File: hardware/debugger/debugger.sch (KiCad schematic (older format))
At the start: 23 parts, among them J1 DB37_Male, J2 DB37_Male, U1 Teensy3.6, U10 PI6C49CB04AQ, U11 PI6C49CB04AQ, U2 SN74CBTLV3257PWR, U3 SN74CBTLV3257PWR, U4 SN74CBTLV3257PWR, U5 SN74CBTLV3257PWR, U6 SN74CBTLV3257PWR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

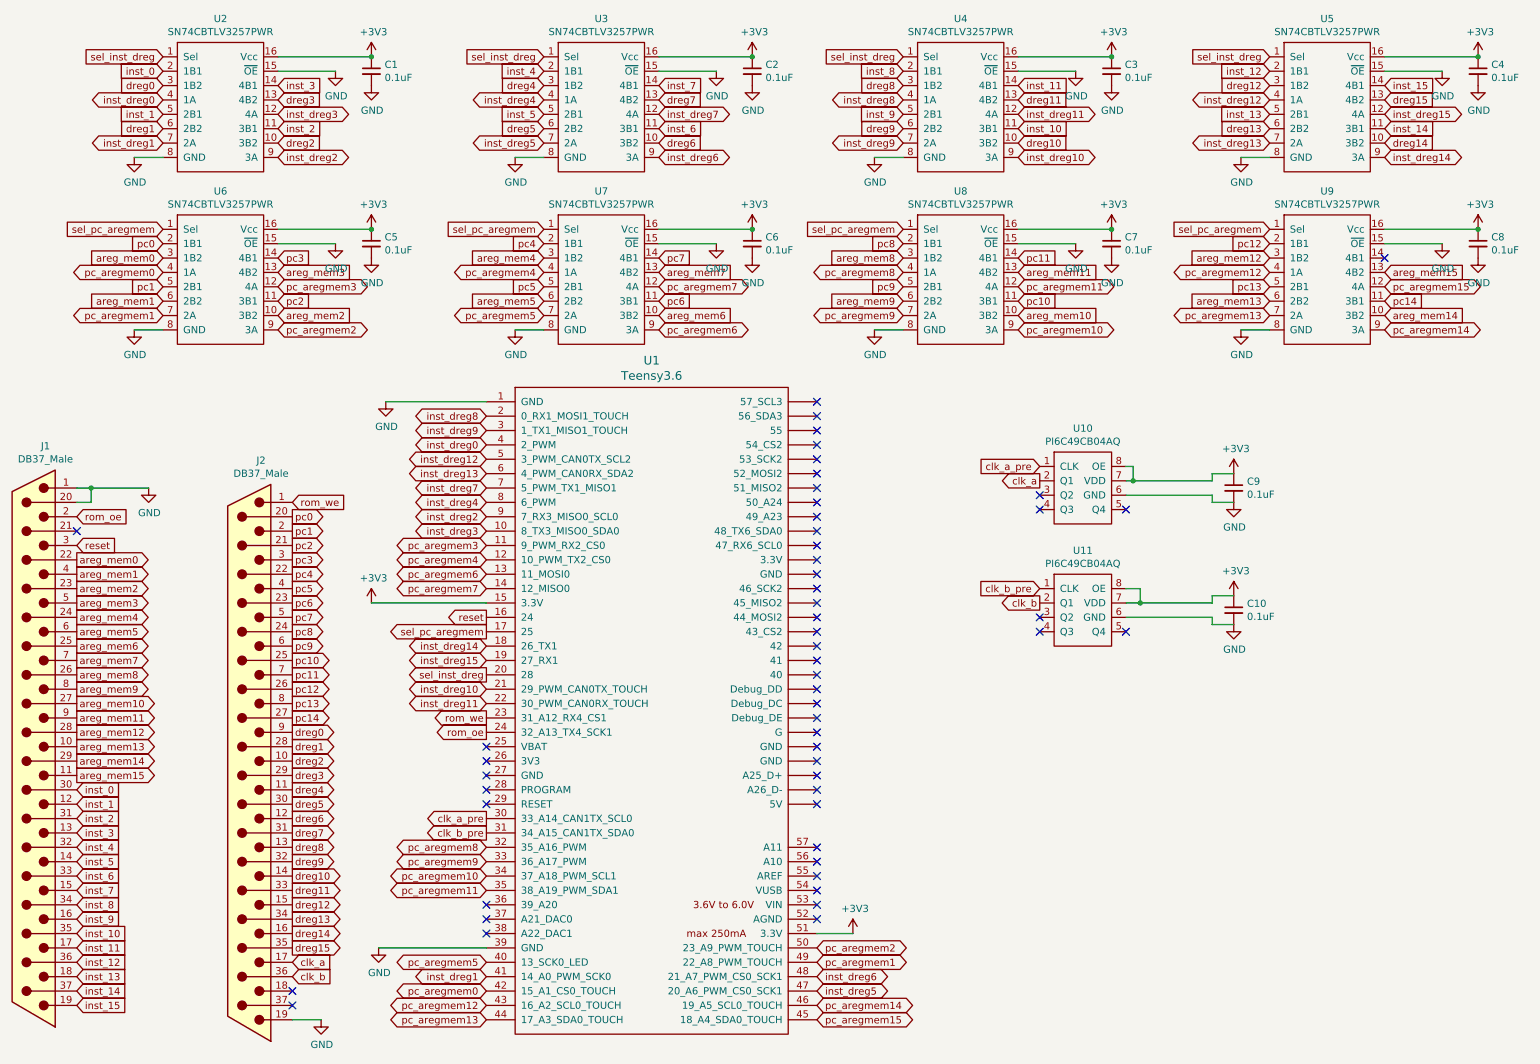
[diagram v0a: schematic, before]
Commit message: Debugger updated to Teensy 4.1 with magjack for ethernet. Updated motherboard<>debugger pinout to include 3.3v source
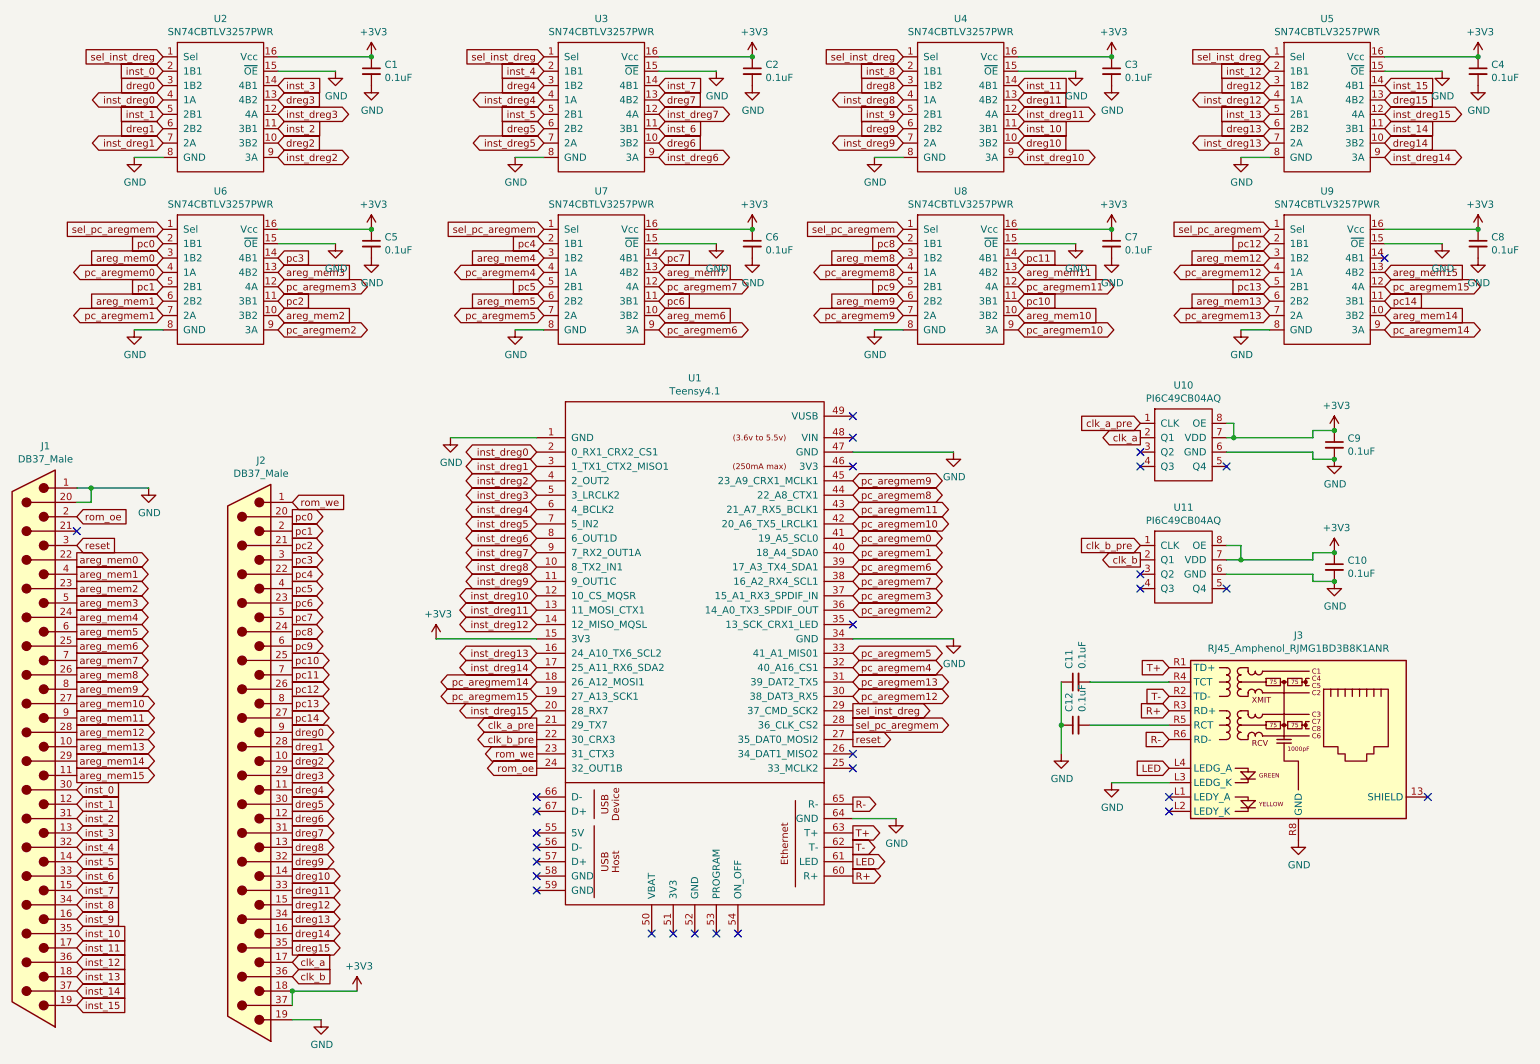
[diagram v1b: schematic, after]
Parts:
- removed U1: Teensy3.6, nandirl logo:Teensy35_36, symbol teensy:Teensy3.6
- added C11, C12: 0.1uF, Capacitor_SMD:C_1206_3216Metric, symbol Device:C_Small
- added J3: RJ45_Amphenol_RJMG1BD3B8K1ANR, Connector_RJ:RJ45_Amphenol_RJMG1BD3B8K1ANR, symbol Connector:RJ45_Amphenol_RJMG1BD3B8K1ANR
- added U1: Teensy4.1, nandirl logo:Teensy41, symbol teensy:Teensy4.1
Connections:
- net +3V3: now also J2.18, J2.37, U1.15 (3V3)
- net GND: now also C11.1, C12.1, J3.L3 (LEDG_K), J3.R8 (GND), U1.1 (GND), U1.34 (GND), U1.47 (GND), U1.64 (GND)
- net clk_a_pre: now also U1.21 (29_TX7)
- net clk_b_pre: now also U1.22 (30_CRX3)
- net inst_dreg0: now also U1.2 (0_RX1_CRX2_CS1)
- net inst_dreg1: now also U1.3 (1_TX1_CTX2_MISO1)
- net inst_dreg10: now also U1.12 (10_CS_MQSR)
- net inst_dreg11: now also U1.13 (11_MOSI_CTX1)
- net inst_dreg12: now also U1.14 (12_MISO_MQSL)
- net inst_dreg13: now also U1.16 (24_A10_TX6_SCL2)
- net inst_dreg14: now also U1.17 (25_A11_RX6_SDA2)
- net inst_dreg15: now also U1.20 (28_RX7)
- net inst_dreg2: now also U1.4 (2_OUT2)
- net inst_dreg3: now also U1.5 (3_LRCLK2)
- net inst_dreg4: now also U1.6 (4_BCLK2)
- net inst_dreg5: now also U1.7 (5_IN2)
- net inst_dreg6: now also U1.8 (6_OUT1D)
- net inst_dreg7: now also U1.9 (7_RX2_OUT1A)
- net inst_dreg8: now also U1.10 (8_TX2_IN1)
- net inst_dreg9: now also U1.11 (9_OUT1C)
- net pc_aregmem0: now also U1.41 (19_A5_SCL0)
- net pc_aregmem1: now also U1.40 (18_A4_SDA0)
- net pc_aregmem10: now also U1.42 (20_A6_TX5_LRCLK1)
- net pc_aregmem11: now also U1.43 (21_A7_RX5_BCLK1)
- net pc_aregmem12: now also U1.30 (38_DAT3_RX5)
- net pc_aregmem13: now also U1.31 (39_DAT2_TX5)
- net pc_aregmem14: now also U1.18 (26_A12_MOSI1)
- net pc_aregmem15: now also U1.19 (27_A13_SCK1)
- net pc_aregmem2: now also U1.36 (14_A0_TX3_SPDIF_OUT)
- net pc_aregmem3: now also U1.37 (15_A1_RX3_SPDIF_IN)
- net pc_aregmem4: now also U1.32 (40_A16_CS1)
- net pc_aregmem5: now also U1.33 (41_A1_MIS01)
- net pc_aregmem6: now also U1.39 (17_A3_TX4_SDA1)
- net pc_aregmem7: now also U1.38 (16_A2_RX4_SCL1)
- net pc_aregmem8: now also U1.44 (22_A8_CTX1)
- net pc_aregmem9: now also U1.45 (23_A9_CRX1_MCLK1)
- net reset: now also U1.27 (35_DAT0_MOSI2)
- net rom_oe: now also U1.24 (32_OUT1B)
- net rom_we: now also U1.23 (31_CTX3)
- net sel_inst_dreg: now also U1.29 (37_CMD_SCK2)
- net sel_pc_aregmem: now also U1.28 (36_CLK_CS2)
- new net: C11.2, J3.R4 (TCT)
- new net: C12.2, J3.R5 (RCT)
- new net LED: J3.L4 (LEDG_A), U1.61 (LED)
- new net R+: J3.R3 (RD+), U1.60 (R+)
- new net R-: J3.R6 (RD-), U1.65 (R-)
- new net T+: J3.R1 (TD+), U1.63 (T+)
- new net T-: J3.R2 (TD-), U1.62 (T-)
- no-connect marks 53 -> 29
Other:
- moved on the sheet: C10, C9, U10, U11
